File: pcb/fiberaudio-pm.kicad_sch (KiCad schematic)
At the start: 7 parts, among them J1 Conn_01x06, J2 PLT237/T10WH, J3 PLR237/T10BK

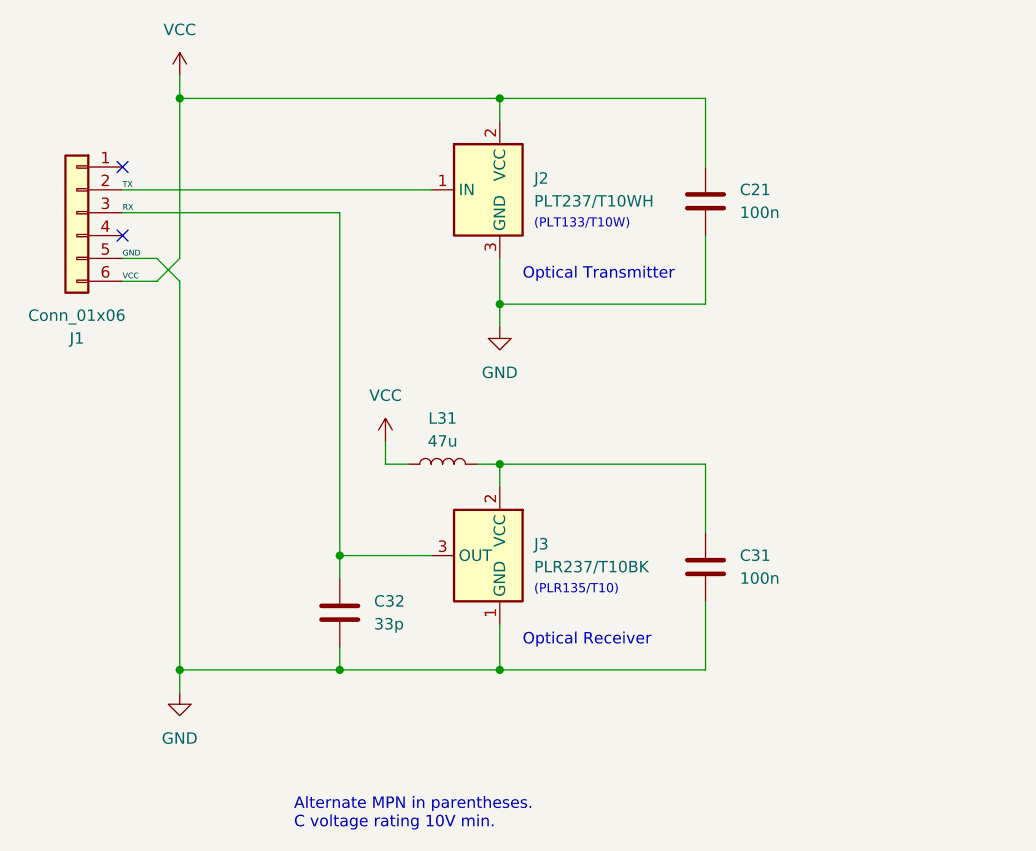
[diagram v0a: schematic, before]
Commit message: Fixed pin-swap on J3; Updated to Rev.2; Updated documentation
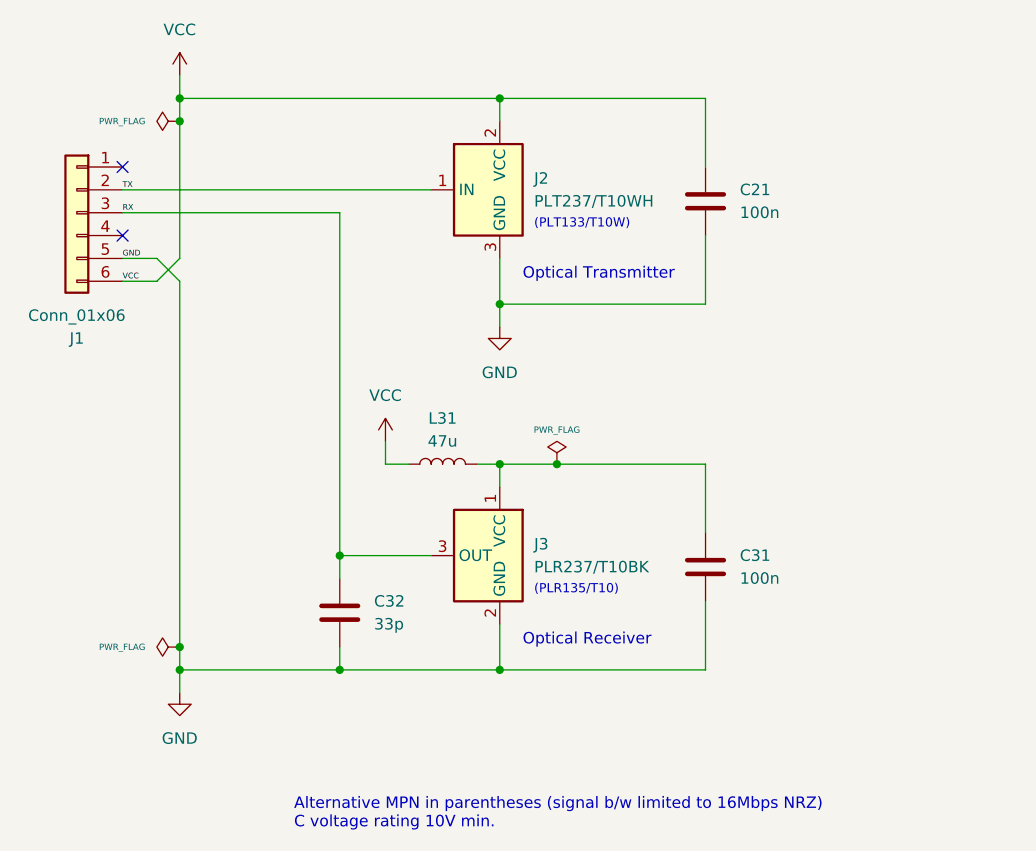
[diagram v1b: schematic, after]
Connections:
- net GND: now also J3.2 (GND); no longer J3.1 (GND)
- net at C31.1, L31.2: now also J3.1 (VCC); no longer J3.2 (VCC)
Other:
- note added: "Alternative MPN in parentheses (signal b/w limited to 16Mbps NRZ) C voltage rating 10V min."
- note removed: "Alternate MPN in parentheses. C voltage rating 10V min."
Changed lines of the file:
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@@
     (title "fiberaudio-pm")
     (date "2024-01-22")
-    (rev "1")
+    (rev "2")
     (company "https://github.com/islandcontroller/fiberaudio-pm")
   )
@@
   (junction (at 78.74 27.94) (diameter 0) (color 0 0 0 0)
   )
+  (junction (at 96.52 78.74) (diameter 0) (color 0 0 0 0)
+  )
+  (junction (at 78.74 30.48) (diameter 0) (color 0 0 0 0)
+  )
+  (junction (at 120.65 68.58) (diameter 0) (color 0 0 0 0)
+  )
+  (junction (at 114.3 91.44) (diameter 0) (color 0 0 0 0)
+  )
+  (junction (at 78.74 91.44) (diameter 0) (color 0 0 0 0)
+  )
   (junction (at 96.52 91.44) (diameter 0) (color 0 0 0 0)
   )
-  (junction (at 96.52 78.74) (diameter 0) (color 0 0 0 0)
-  )
-  (junction (at 114.3 91.44) (diameter 0) (color 0 0 0 0)
-  )
   (junction (at 114.3 27.94) (diameter 0) (color 0 0 0 0)
   )
   (junction (at 114.3 50.8) (diameter 0) (color 0 0 0 0)
   )
-  (junction (at 78.74 91.44) (diameter 0) (color 0 0 0 0)
+  (junction (at 78.74 88.9) (diameter 0) (color 0 0 0 0)
   )
   (no_connect (at 72.39 35.56))
@@
     (stroke (width 0) (type default))
   )
+  (wire (pts (xy 78.74 30.48) (xy 78.74 45.72))
+    (stroke (width 0) (type default))
+  )
   (wire (pts (xy 137.16 76.2) (xy 137.16 68.58))
     (stroke (width 0) (type default))
@@
     (stroke (width 0) (type default))
   )
-  (wire (pts (xy 137.16 68.58) (xy 114.3 68.58))
+  (wire (pts (xy 120.65 68.58) (xy 137.16 68.58))
+    (stroke (width 0) (type default))
+  )
+  (wire (pts (xy 114.3 68.58) (xy 120.65 68.58))
     (stroke (width 0) (type default))
   )
@@
     (stroke (width 0) (type default))
   )
+  (wire (pts (xy 78.74 91.44) (xy 78.74 93.98))
+    (stroke (width 0) (type default))
+  )
   (wire (pts (xy 114.3 50.8) (xy 137.16 50.8))
     (stroke (width 0) (type default))
@@
     (stroke (width 0) (type default))
   )
-  (wire (pts (xy 78.74 91.44) (xy 78.74 93.98))
-    (stroke (width 0) (type default))
-  )
   (wire (pts (xy 78.74 27.94) (xy 114.3 27.94))
     (stroke (width 0) (type default))
@@
     (stroke (width 0) (type default))
   )
+  (wire (pts (xy 78.74 88.9) (xy 78.74 91.44))
+    (stroke (width 0) (type default))
+  )
   (wire (pts (xy 137.16 27.94) (xy 137.16 35.56))
     (stroke (width 0) (type default))
@@
     (stroke (width 0) (type default))
   )
-  (wire (pts (xy 78.74 27.94) (xy 78.74 45.72))
+  (wire (pts (xy 78.74 48.26) (xy 78.74 88.9))
     (stroke (width 0) (type default))
   )
@@
     (stroke (width 0) (type default))
   )
-  (wire (pts (xy 78.74 48.26) (xy 78.74 91.44))
-    (stroke (width 0) (type default))
-  )
   (wire (pts (xy 137.16 50.8) (xy 137.16 43.18))
     (stroke (width 0) (type default))
@@
     (stroke (width 0) (type default))
   )
+  (wire (pts (xy 78.74 27.94) (xy 78.74 30.48))
+    (stroke (width 0) (type default))
+  )
   (text "Optical Transmitter" (at 116.84 48.26 0)
     (effects (font (size 1.27 1.27)) (justify left bottom))
@@
     (effects (font (size 1.27 1.27)) (justify left bottom))
   )
-  (text "Alternate MPN in parentheses.\nC voltage rating 10V min."
+  (text "Alternative MPN in parentheses (signal b/w limited to 16Mbps NRZ)\nC voltage rating 10V min."
     (at 91.44 109.22 0)
     (effects (font (size 1.27 1.27)) (justify left bottom))
@@
     (effects (font (size 0.635 0.635)) (justify left bottom))
   )
+  (netclass_flag "" (length 2.54) (shape diamond) (at 114.3 68.58 0)
+    (effects (font (size 1.27 1.27)) (justify left bottom))
+    (property "Netclass" "Power" (at 114.3 64.77 0)
+      (effects (font (size 0.7 0.7) italic))
+    )
+  )
+  (netclass_flag "" (length 2.54) (shape diamond) (at 78.74 27.94 90)
+    (effects (font (size 1.27 1.27)) (justify left bottom))
+    (property "Netclass" "Power" (at 74.93 27.94 0)
+      (effects (font (size 0.7 0.7) italic) (justify right))
+    )
+  )
   (netclass_flag "" (length 2.54) (shape diamond) (at 78.74 91.44 90)
     (effects (font (size 1.27 1.27)) (justify left bottom))
-    (property "Netclass" "Power" (at 73.66 91.44 0) (do_not_autoplace)
-      (effects (font (size 0.7 0.7) italic))
-    )
-  )
-  (netclass_flag "" (length 2.54) (shape diamond) (at 114.3 27.94 0) (fields_autoplaced)
-    (effects (font (size 1.27 1.27)) (justify left bottom))
-    (property "Netclass" "Power" (at 115.5065 25.4 0)
-      (effects (font (size 0.7 0.7) italic) (justify left))
-    )
-  )
-  (netclass_flag "" (length 2.54) (shape diamond) (at 114.3 68.58 0) (fields_autoplaced)
-    (effects (font (size 1.27 1.27)) (justify left bottom))
-    (property "Netclass" "Power" (at 115.5065 66.04 0)
-      (effects (font (size 0.7 0.7) italic) (justify left))
+    (property "Netclass" "Power" (at 74.93 91.44 0) (do_not_autoplace)
+      (effects (font (size 0.7 0.7) italic) (justify right))
+    )
+  )
+  (symbol (lib_id "power:PWR_FLAG") (at 78.74 30.48 90) (unit 1)
+    (in_bom yes) (on_board yes) (dnp no) (fields_autoplaced)
+    (property "Reference" "#FLG03" (at 76.835 30.48 0)
+      (effects (font (size 1.27 1.27)) hide)
+    )
+    (property "Value" "PWR_FLAG" (at 74.93 30.48 90)
+      (effects (font (size 0.7 0.7)) (justify left))
+    )
+    (property "Footprint" "" (at 78.74 30.48 0)
+      (effects (font (size 1.27 1.27)) hide)
+    )
+    (property "Datasheet" "~" (at 78.74 30.48 0)
+      (effects (font (size 1.27 1.27)) hide)
+    )
+    (pin "1")
+    (instances
+      (project "fiberaudio-pm"
+        (path "/9fea33af-33d0-45a3-bc1c-54f82b91c024"
+          (reference "#FLG03") (unit 1)
+        )
+      )
     )
   )
@@
     )
   )
+  (symbol (lib_id "power:PWR_FLAG") (at 120.65 68.58 0) (unit 1)
+    (in_bom yes) (on_board yes) (dnp no) (fields_autoplaced)
+    (property "Reference" "#FLG01" (at 120.65 66.675 0)
+      (effects (font (size 1.27 1.27)) hide)
+    )
+    (property "Value" "PWR_FLAG" (at 120.65 64.77 0)
+      (effects (font (size 0.7 0.7)))
+    )
+    (property "Footprint" "" (at 120.65 68.58 0)
+      (effects (font (size 1.27 1.27)) hide)
+    )
+    (property "Datasheet" "~" (at 120.65 68.58 0)
+      (effects (font (size 1.27 1.27)) hide)
+    )
+    (pin "1")
+    (instances
+      (project "fiberaudio-pm"
+        (path "/9fea33af-33d0-45a3-bc1c-54f82b91c024"
+          (reference "#FLG01") (unit 1)
+        )
+      )
+    )
+  )
   (symbol (lib_id "Device:C") (at 137.16 80.01 0) (unit 1)
     (in_bom yes) (on_board yes) (dnp no) (fields_autoplaced)
@@
       (effects (font (size 1.27 1.27)) hide)
     )
-    (property "Datasheet" "" (at 138.43 30.48 0)
+    (property "Datasheet" "../doc/plt237_t10wh.pdf" (at 138.43 30.48 0)
       (effects (font (size 1.27 1.27)) hide)
     )
@@
         (path "/9fea33af-33d0-45a3-bc1c-54f82b91c024"
           (reference "L31") (unit 1)
+        )
+      )
+    )
+  )
+  (symbol (lib_id "power:PWR_FLAG") (at 78.74 88.9 90) (unit 1)
+    (in_bom yes) (on_board yes) (dnp no) (fields_autoplaced)
+    (property "Reference" "#FLG02" (at 76.835 88.9 0)
+      (effects (font (size 1.27 1.27)) hide)
+    )
+    (property "Value" "PWR_FLAG" (at 74.93 88.9 90)
+      (effects (font (size 0.7 0.7)) (justify left))
+    )
+    (property "Footprint" "" (at 78.74 88.9 0)
+      (effects (font (size 1.27 1.27)) hide)
+    )
+    (property "Datasheet" "~" (at 78.74 88.9 0)
+      (effects (font (size 1.27 1.27)) hide)
+    )
+    (pin "1")
+    (instances
+      (project "fiberaudio-pm"
+        (path "/9fea33af-33d0-45a3-bc1c-54f82b91c024"
+          (reference "#FLG02") (unit 1)
         )
       )
@@
       (effects (font (size 1.27 1.27)) hide)
     )
-    (property "Datasheet" "" (at 87.63 71.12 0)
-      (effects (font (size 1.27 1.27)) hide)
-    )
+    (property "Datasheet" "../doc/plr237_t10bk.pdf" (at 87.63 71.12 0)
+      (effects (font (size 1.27 1.27)) hide)
+    )
